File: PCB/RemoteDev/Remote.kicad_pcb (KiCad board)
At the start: 2 copper layers, 70 x 70 mm, 90 parts, among them J1 LCD, J2 DC, J3 TEMP, J4 LCD, J5 Reset, J6 USB-C-Socket-H, J7 TC2030-USB-NL-DS, T1 T3902_MEMS_Mic, U1 ESP32-S3-MINI-1, U2 SCD41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

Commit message: Latest renders
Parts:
- R9: footprint RevK:R_0402 -> RevK:R_0201

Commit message: wider
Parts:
- D19, D20: value MBR0530 -> DKS22; footprint RevK:D_SOD-123 -> RevK:D_SOD-123FL
- moved J6 0.50 mm to (100.0, 104.1)
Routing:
- net +3.3V: track 258.8 -> 261.5 mm
- net LED: track 25.8 -> 24.8 mm

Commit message: Library update
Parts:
- D19, D20: value DKS22 -> DKS34
- U9: value TPS562243 -> TPS562246

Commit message: MPNs
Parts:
- R9: footprint RevK:R_0201 -> RevK:R_0402
- moved R9 0.10 mm to (85.6, 113.5)

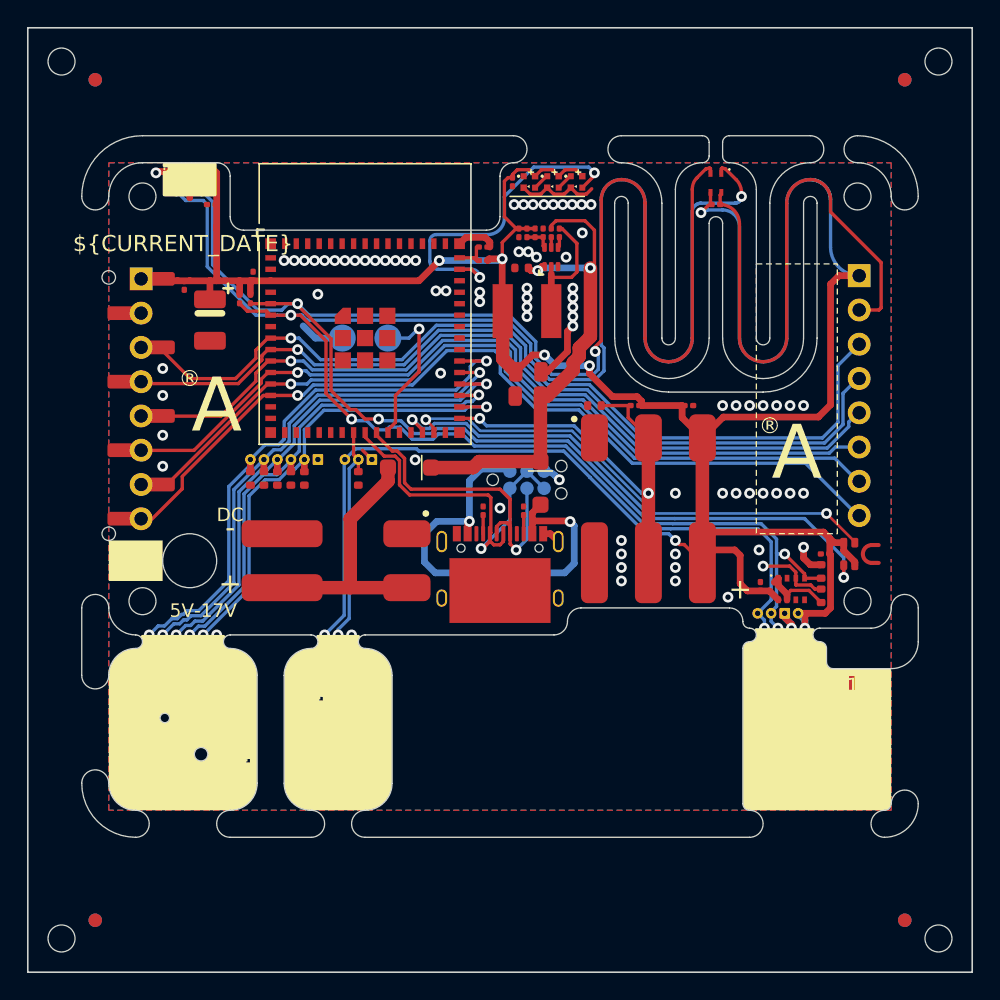
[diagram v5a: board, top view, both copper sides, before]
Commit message: Clearing inductror
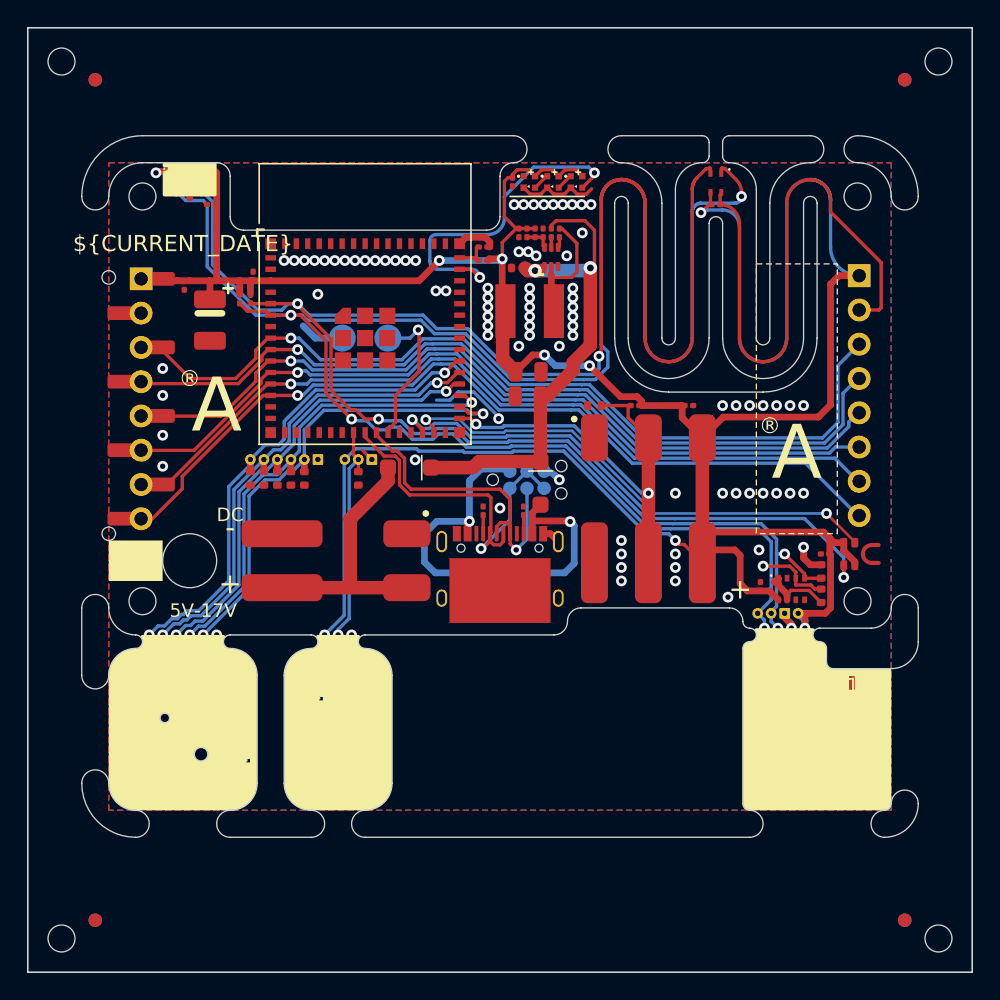
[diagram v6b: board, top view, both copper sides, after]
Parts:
- moved C21 0.25 mm to (101.3, 82.8)
- moved L2 0.20 mm to (102.2, 86.0)
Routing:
- net W: track 55.6 -> 50.9 mm
- net S: track 48.5 -> 44.5 mm
- net E: track 48.3 -> 45.1 mm
- net RST: track 62.0 -> 60.4 mm
- net DIN: track 65.5 -> 63.9 mm
- net CS: track 61.7 -> 60.1 mm
- net CLK: track 63.1 -> 61.5 mm
- net DC: track 61.0 -> 59.4 mm
- net BL: track 63.8 -> 62.3 mm
- net GND: track 96.1 -> 97.2 mm, vias 93 -> 102
- net N: track 47.0 -> 45.9 mm
- net SCL: track 156.9 -> 155.9 mm
- net VDC: track 36.6 -> 37.4 mm
- net +3.3V: track 261.5 -> 261.0 mm
